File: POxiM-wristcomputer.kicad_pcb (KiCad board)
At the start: 4 copper layers, 38.1 x 22.6 mm, 58 parts, among them J1 USB_B_Micro, J2 AudioJack4_Ground, U1 LM321, U2 STM8S003F3P

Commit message: big chungus
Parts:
- moved D11 9.49 mm to (117.7, 132.4)
- moved D9 9.13 mm to (117.7, 124.4)
- moved D13 8.92 mm to (113.7, 136.5)
- moved D19 8.28 mm to (113.7, 128.4)
- moved D7 8.12 mm to (113.7, 120.4)
- moved D15 7.59 mm to (109.7, 132.4)
- moved H1 7.32 mm to (107.2, 137.5)
- moved D17 7.14 mm to (109.7, 124.4)
- moved R6 6.61 mm to (107.2, 128.5)
- moved D25 6.21 mm to (104.7, 132.4)
- moved D27 5.85 mm to (100.7, 136.4)
- moved D23 5.65 mm to (104.7, 124.4)
- moved J1 5.44 mm to (72.1, 135.2), turned to 270 degrees
- moved D30 4.85 mm to (100.7, 128.4)
- moved D21 4.62 mm to (100.7, 120.4)
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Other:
- board size 38.1 x 22.6 mm -> 48.1 x 27.3 mm

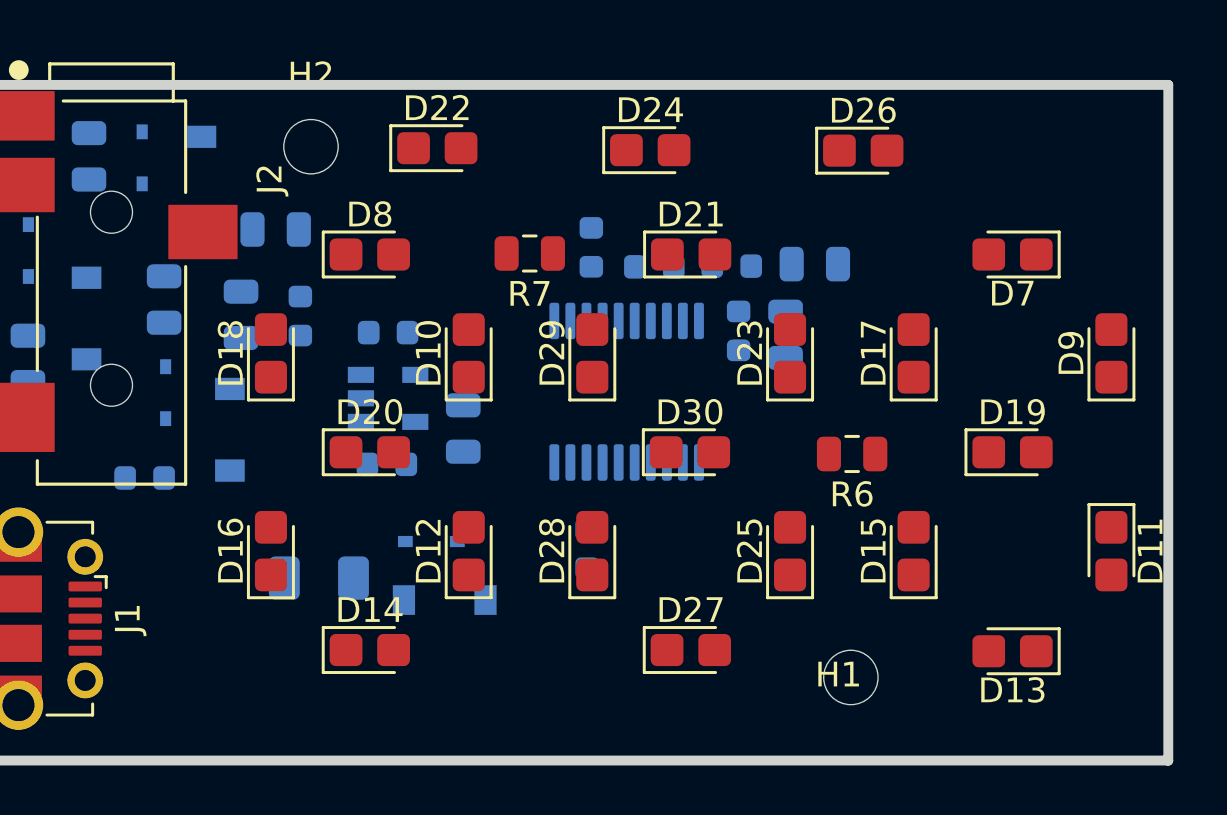
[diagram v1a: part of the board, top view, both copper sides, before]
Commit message: Draw segments on user layer
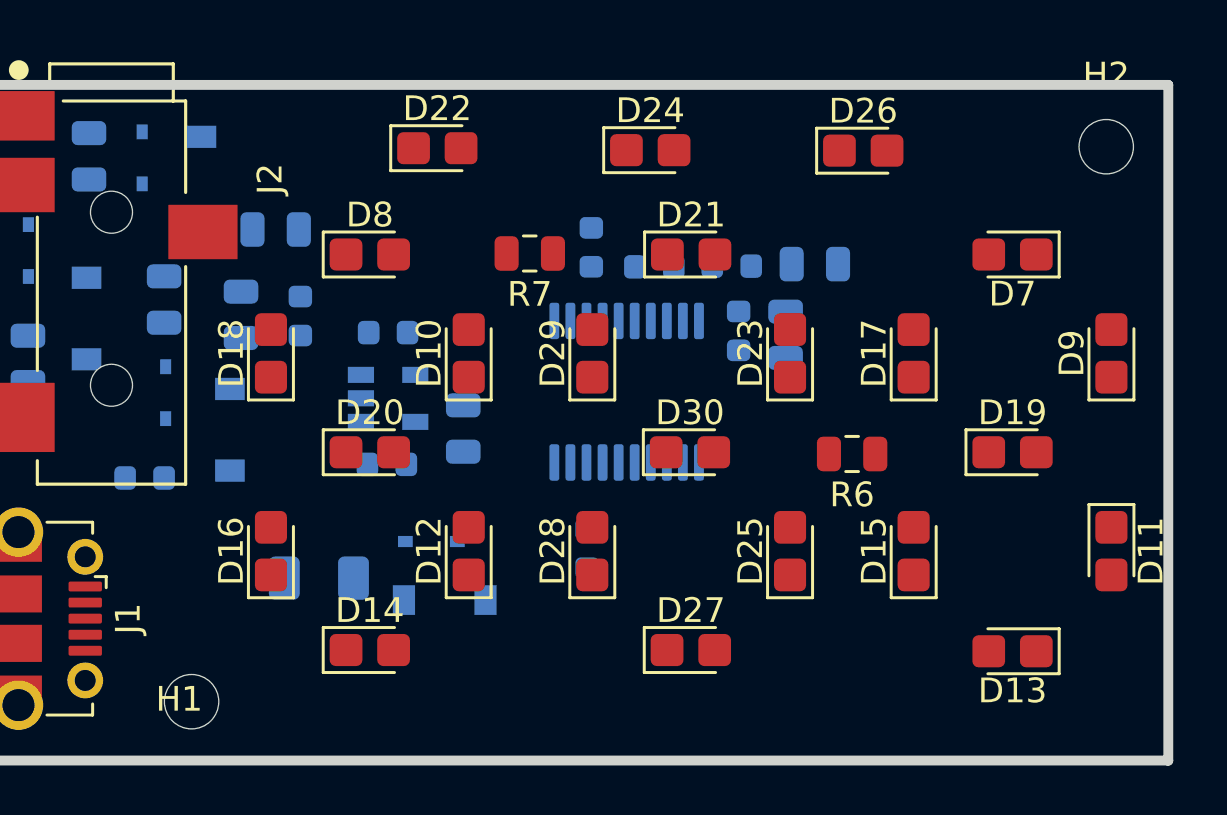
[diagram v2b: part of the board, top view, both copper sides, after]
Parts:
- moved H2 32.2 mm to (117.5, 116.0)
- moved H1 26.7 mm to (80.5, 138.5)
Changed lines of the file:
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@@
-(kicad_pcb (version 20171130) (host pcbnew 5.1.6-c6e7f7d~86~ubuntu18.04.1)
+(kicad_pcb (version 20171130) (host pcbnew "(5.1.0-0)")
   (general
     (thickness 1.6)
-    (drawings 4)
+    (drawings 25)
     (tracks 0)
     (zones 0)
@@
   )
   (module MountingHole:MountingHole_2.2mm_M2_DIN965 (layer F.Cu)
-    (at 85.33 116.05)
+    (at 117.5 116.05)
     (descr "Mounting Hole 2.2mm, no annular, M2, DIN965")
     (tags "mounting hole 2.2mm no annular m2 din965")
@@
   )
   (module MountingHole:MountingHole_2.2mm_M2_DIN965 (layer F.Cu)
-    (at 107.17 137.52)
+    (at 80.5 138.5)
     (descr "Mounting Hole 2.2mm, no annular, M2, DIN965")
     (tags "mounting hole 2.2mm no annular m2 din965")
@@
     )
   )
+  (gr_poly (pts (xy 83.7 135.9) (xy 84.2 135.4) (xy 84.2 129.4) (xy 83.7 128.9) (xy 83.2 129.4) (xy 83.2 135.4)) (layer Dwgs.User) (width 0.1))
+  (gr_poly (pts (xy 91.2 120.4) (xy 90.7 119.9) (xy 84.7 119.9) (xy 84.2 120.4) (xy 84.7 120.9) (xy 90.7 120.9)) (layer Dwgs.User) (width 0.1))
+  (gr_poly (pts (xy 91.2 136.4) (xy 90.7 135.9) (xy 84.7 135.9) (xy 84.2 136.4) (xy 84.7 136.9) (xy 90.7 136.9)) (layer Dwgs.User) (width 0.1))
+  (gr_poly (pts (xy 91.7 135.9) (xy 92.2 135.4) (xy 92.2 129.4) (xy 91.7 128.9) (xy 91.2 129.4) (xy 91.2 135.4)) (layer Dwgs.User) (width 0.1))
+  (gr_poly (pts (xy 83.7 120.9) (xy 83.2 121.4) (xy 83.2 127.4) (xy 83.7 127.9) (xy 84.2 127.4) (xy 84.2 121.4)) (layer Dwgs.User) (width 0.1))
+  (gr_poly (pts (xy 91.7 120.9) (xy 91.2 121.4) (xy 91.2 127.4) (xy 91.7 127.9) (xy 92.2 127.4) (xy 92.2 121.4)) (layer Dwgs.User) (width 0.1))
+  (gr_poly (pts (xy 91.2 128.4) (xy 90.7 127.9) (xy 84.7 127.9) (xy 84.2 128.4) (xy 84.7 128.9) (xy 90.7 128.9)) (layer Dwgs.User) (width 0.1))
+  (gr_poly (pts (xy 96.7 135.9) (xy 97.2 135.4) (xy 97.2 129.4) (xy 96.7 128.9) (xy 96.2 129.4) (xy 96.2 135.4)) (layer Dwgs.User) (width 0.1))
+  (gr_poly (pts (xy 104.2 120.4) (xy 103.7 119.9) (xy 97.7 119.9) (xy 97.2 120.4) (xy 97.7 120.9) (xy 103.7 120.9)) (layer Dwgs.User) (width 0.1))
+  (gr_poly (pts (xy 104.2 136.4) (xy 103.7 135.9) (xy 97.7 135.9) (xy 97.2 136.4) (xy 97.7 136.9) (xy 103.7 136.9)) (layer Dwgs.User) (width 0.1))
+  (gr_poly (pts (xy 104.7 135.9) (xy 105.2 135.4) (xy 105.2 129.4) (xy 104.7 128.9) (xy 104.2 129.4) (xy 104.2 135.4)) (layer Dwgs.User) (width 0.1))
+  (gr_poly (pts (xy 96.7 120.9) (xy 96.2 121.4) (xy 96.2 127.4) (xy 96.7 127.9) (xy 97.2 127.4) (xy 97.2 121.4)) (layer Dwgs.User) (width 0.1))
+  (gr_poly (pts (xy 104.7 120.9) (xy 104.2 121.4) (xy 104.2 127.4) (xy 104.7 127.9) (xy 105.2 127.4) (xy 105.2 121.4)) (layer Dwgs.User) (width 0.1))
+  (gr_poly (pts (xy 104.2 128.4) (xy 103.7 127.9) (xy 97.7 127.9) (xy 97.2 128.4) (xy 97.7 128.9) (xy 103.7 128.9)) (layer Dwgs.User) (width 0.1))
+  (gr_poly (pts (xy 117.2 120.4) (xy 116.7 119.9) (xy 110.7 119.9) (xy 110.2 120.4) (xy 110.7 120.9) (xy 116.7 120.9)) (layer Dwgs.User) (width 0.1))
+  (gr_poly (pts (xy 117.7 120.9) (xy 117.2 121.4) (xy 117.2 127.4) (xy 117.7 127.9) (xy 118.2 127.4) (xy 118.2 121.4)) (layer Dwgs.User) (width 0.1))
+  (gr_poly (pts (xy 117.2 136.4) (xy 116.7 135.9) (xy 110.7 135.9) (xy 110.2 136.4) (xy 110.7 136.9) (xy 116.7 136.9)) (layer Dwgs.User) (width 0.1))
+  (gr_poly (pts (xy 117.7 135.9) (xy 118.2 135.4) (xy 118.2 129.4) (xy 117.7 128.9) (xy 117.2 129.4) (xy 117.2 135.4)) (layer Dwgs.User) (width 0.1))
+  (gr_poly (pts (xy 109.7 135.9) (xy 110.2 135.4) (xy 110.2 129.4) (xy 109.7 128.9) (xy 109.2 129.4) (xy 109.2 135.4)) (layer Dwgs.User) (width 0.1))
+  (gr_poly (pts (xy 117.2 128.4) (xy 116.7 127.9) (xy 110.7 127.9) (xy 110.2 128.4) (xy 110.7 128.9) (xy 116.7 128.9)) (layer Dwgs.User) (width 0.1))
+  (gr_poly (pts (xy 109.7 120.9) (xy 109.2 121.4) (xy 109.2 127.4) (xy 109.7 127.9) (xy 110.2 127.4) (xy 110.2 121.4)) (layer Dwgs.User) (width 0.1))
   (gr_line (start 120.01 140.88) (end 71.9 140.88) (layer Edge.Cuts) (width 0.4))
   (gr_line (start 120.01 140.89) (end 120.01 113.55) (layer Edge.Cuts) (width 0.4))

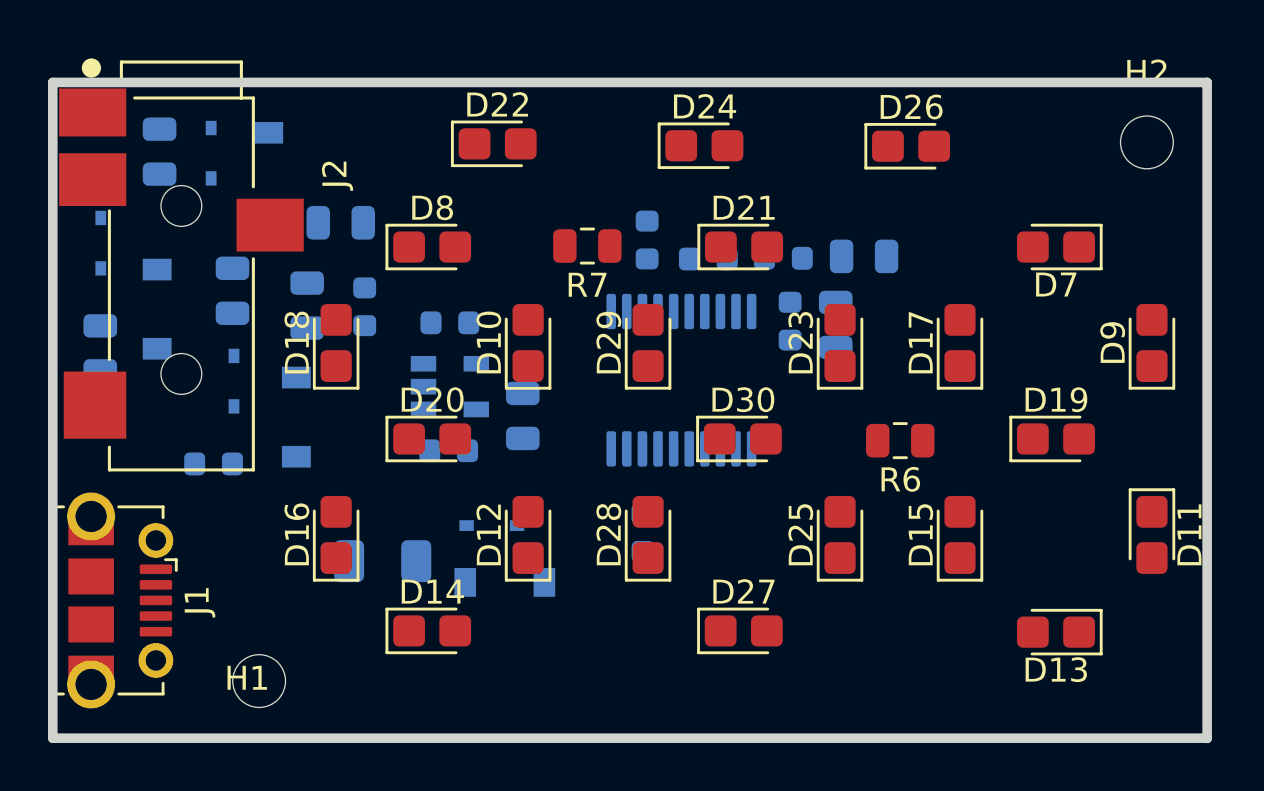
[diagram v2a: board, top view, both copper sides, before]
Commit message: reduce digit spacing and export step
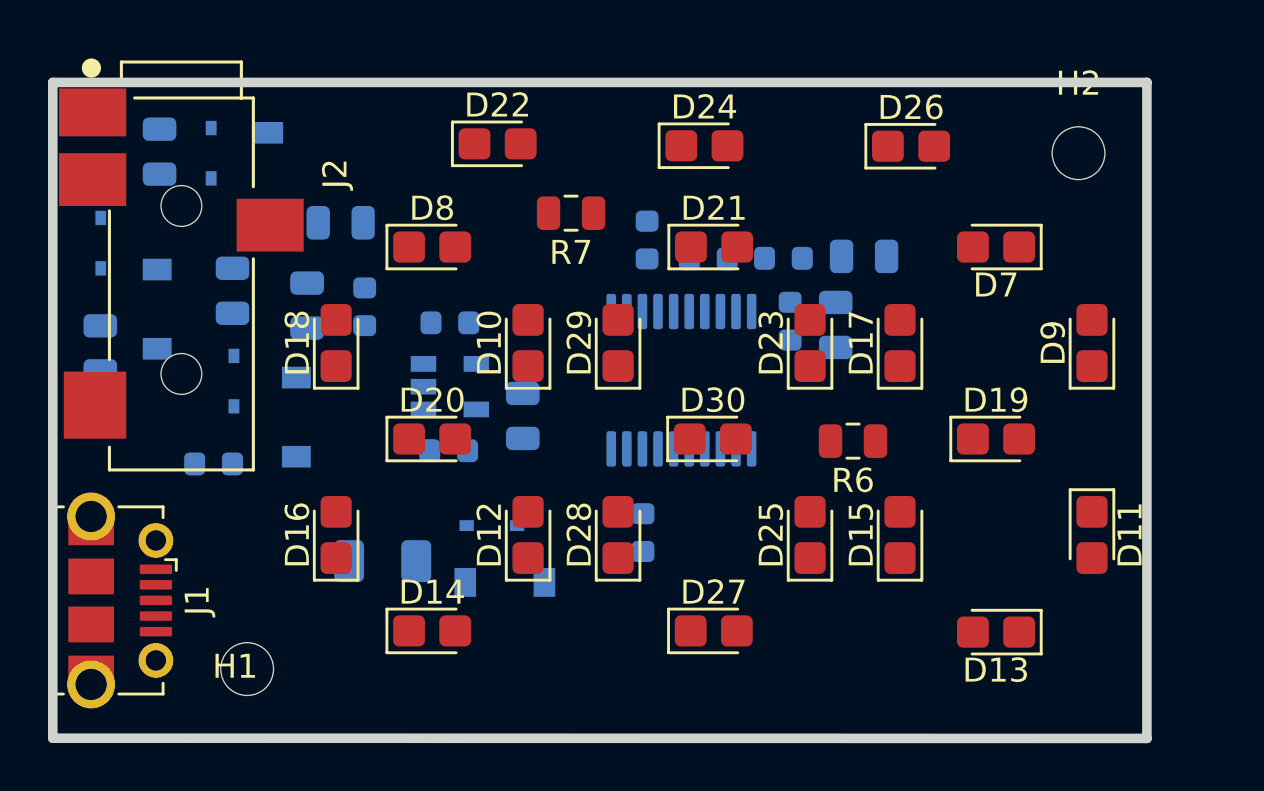
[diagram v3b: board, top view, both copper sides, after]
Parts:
- moved H2 2.89 mm to (114.7, 116.5)
- moved D11 2.50 mm to (115.2, 132.4)
- moved D13 2.50 mm to (111.2, 136.5)
- moved D15 2.50 mm to (107.2, 132.4)
- moved D17 2.50 mm to (107.2, 124.4)
- moved D19 2.50 mm to (111.2, 128.4)
- moved D7 2.50 mm to (111.2, 120.4)
- moved D9 2.50 mm to (115.2, 124.4)
- moved R6 1.97 mm to (105.2, 128.5)
- moved R7 1.53 mm to (93.5, 119.0)
- moved D21 1.25 mm to (99.5, 120.4)
- moved D23 1.25 mm to (103.5, 124.4)
- moved D25 1.25 mm to (103.5, 132.4)
- moved D27 1.25 mm to (99.4, 136.4)
- moved D28 1.25 mm to (95.5, 132.4)
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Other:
- board size 48.1 x 27.3 mm -> 45.6 x 27.3 mm

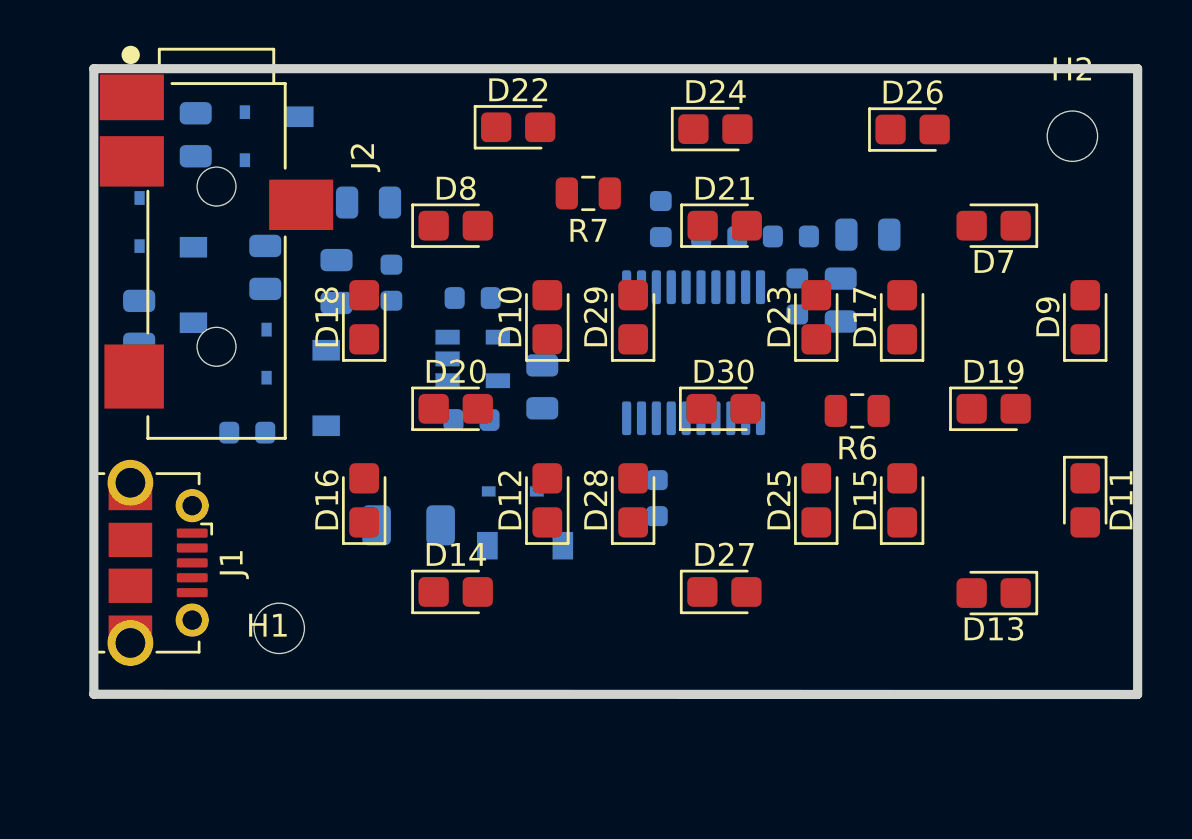
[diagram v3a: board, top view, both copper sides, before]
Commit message: Refactor based on feedback from Daniel
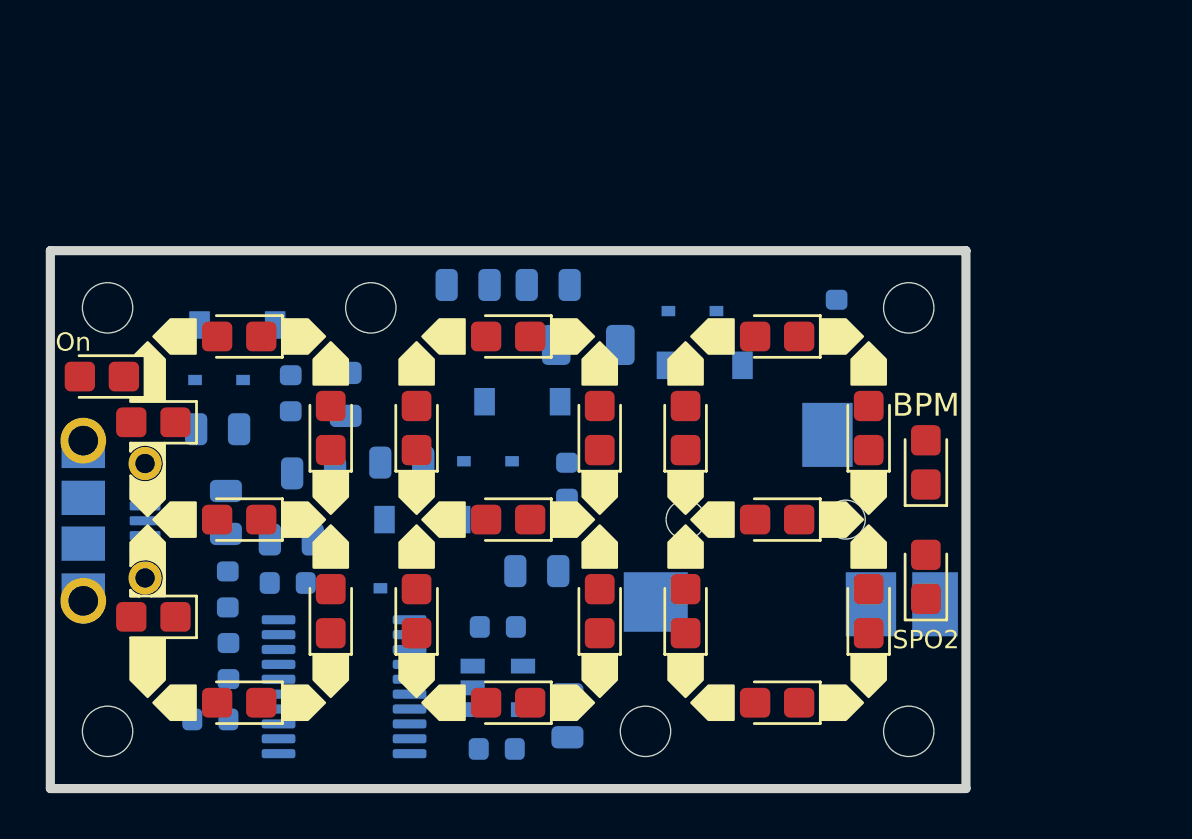
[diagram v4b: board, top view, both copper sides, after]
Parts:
- added H3: MountingHole, MountingHole:MountingHole_2.2mm_M2_DIN965, F.Cu at (107.5, 142.5)
- added H4: MountingHole, MountingHole:MountingHole_2.2mm_M2_DIN965, F.Cu at (72.5, 142.5)
- added H5: AlignmentHole, MountingHole:MountingHole_2.2mm_M2_DIN965, F.Cu at (84.0, 124.0)
- added H6: AlignmentHole, MountingHole:MountingHole_2.2mm_M2_DIN965, F.Cu at (96.0, 142.5)
- J1, J2, R6, R7: moved to B.Cu
- moved FB1 30.6 mm to (77.7, 132.9), turned to 90 degrees
- moved C5 29.4 mm to (77.0, 142.0), turned to 180 degrees
- moved C9 29.0 mm to (77.8, 136.3), turned to 90 degrees
- moved C7 28.3 mm to (77.8, 139.4), turned to 270 degrees
- moved J2 26.7 mm to (101.5, 133.2), turned to 180 degrees
- moved C6 26.2 mm to (80.5, 134.1), turned to 0 degrees
- moved C8 25.5 mm to (80.4, 136.0), turned to 0 degrees
- moved D22 21.2 mm to (72.2, 127.0), turned to 180 degrees
- moved U2 21.1 mm to (82.8, 140.6), turned to 0 degrees
- moved R4 20.5 mm to (91.2, 135.5), turned to 0 degrees
- moved D26 19.5 mm to (108.2, 135.8), turned to 90 degrees
- moved D4 18.6 mm to (83.4, 136.2), turned to 180 degrees
- moved D24 17.2 mm to (108.2, 130.8), turned to 90 degrees
- moved H1 15.9 mm to (72.5, 124.0)
- moved R6 14.6 mm to (91.8, 123.0)
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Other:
- board size 45.6 x 27.3 mm -> 40 x 23.5 mm
- board text added: "BPM"
- board text added: "On"
- board text added: "SPO2"
